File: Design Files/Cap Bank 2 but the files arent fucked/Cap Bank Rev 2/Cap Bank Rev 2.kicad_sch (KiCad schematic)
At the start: 20 parts, among them Q1 2N3904, Q2 2N3904, Q3 2N3904, Q4 2N3904

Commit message: New Cap Bank
wohooo
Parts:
- removed C2: C_Polarized, Library:bigcap, symbol Device:C_Polarized
- added C5: C_Polarized, Library:bigcap2pos, symbol Device:C_Polarized
- added J1: Conn_01x02, Library:xt30, symbol Connector_Generic:Conn_01x02
- C1: footprint Library:bigcap -> Library:bigcap2pos
- C3: footprint Library:bigcap -> Library:bigcap2neg
- C4: footprint Library:bigcap -> Library:smallcap
- C7: footprint Library:smallcap -> Library:bigcap2neg
- Q1, Q2, Q3, Q4: footprint Package_TO_SOT_THT:TO-92_Inline -> Library:2n3904
- renumbered C5 to C2
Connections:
- net V_IN: now also Q1.3 (C), R1.2, J1.1 (Pin_1); no longer C1.2, C2.2, C3.1, C3.2, C4.1, C4.2, C6.1, C6.2, C7.1, C7.2, C8.1, C8.2, Q1.2 (B), Q2.2 (B), Q3.2 (B), Q4.2 (B), R1.1, R2.1, R3.1, R4.1, R5.1, R6.1, R7.1, R8.1
- net at Q2.1 (E), R4.2: now also C3.2, C4.2, C6.1, Q3.3 (C), R5.2, C5.1
- net at Q4.3 (C), R7.2: now also C6.2, C7.1, C8.1, Q3.1 (E), R6.2, C5.2
- net at Q2.3 (C), R3.2: now also C1.2, C2.2, C3.1, C4.1, Q1.1 (E), R2.2
- net GND: now reaches Q4.1 (E), R8.2
- net GND: now also C7.2, C8.2, J1.2 (Pin_2)
- new net: Q3.2 (B), R5.1, R6.1
- new net: Q2.2 (B), R3.1, R4.1
- new net: Q1.2 (B), R1.1, R2.1
- new net: Q4.2 (B), R7.1, R8.1
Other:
- moved on the sheet: C1, Q1, R1, R2

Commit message: updated again!!!
ship it!
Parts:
- removed C2, C4, C6, C8: C_Polarized, Library:smallcap, symbol Device:C_Polarized
- added J2: Conn_01x02, Connector_AMASS:AMASS_XT30U-F_1x02_P5.0mm_Vertical, symbol Connector_Generic:Conn_01x02
- C1, C5: footprint Library:bigcap2pos -> Library:bigcap
- C3, C7: footprint Library:bigcap2neg -> Library:bigcap
- J1: footprint Library:xt30 -> Connector_AMASS:AMASS_XT30U-M_1x02_P5.0mm_Vertical
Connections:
- net GND: now also J1.1 (Pin_1), J2.1 (Pin_1); no longer J1.2 (Pin_2)
- net V_IN: now also J1.2 (Pin_2), J2.2 (Pin_2); no longer J1.1 (Pin_1)
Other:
- moved on the sheet: J1

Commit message: new bjt
who dis
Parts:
- removed Q1, Q2, Q3, Q4: 2N3904, Library:2n3904, symbol Transistor_BJT:2N3904
- added D1: LED, LED_THT:LED_D3.0mm_Clear, symbol Device:LED
- added Q1, Q2, Q3, Q4: TIP31, Library:tip31, symbol Transistor_BJT:TIP41
- added R9: 1000, Resistor_THT:R_Axial_DIN0207_L6.3mm_D2.5mm_P7.62mm_Horizontal, symbol Device:R
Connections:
- net GND: now also D1.1 (K), Q4.3 (E)
- net V_IN: now also Q1.2 (C), R9.1
- net at C7.1, R7.2: now also Q4.2 (C); no longer C5.2, R6.2
- net at R5.1, R6.1: now also Q3.1 (B)
- net at C5.1, R5.2: now also Q3.2 (C); no longer C3.2, R4.2
- net at R3.1, R4.1: now also Q2.1 (B)
- net at C3.1, R3.2: now also Q2.2 (C); no longer C1.2, R2.2
- net at R1.1, R2.1: now also Q1.1 (B)
- net at R7.1, R8.1: now also Q4.1 (B)
- new net: C5.2, Q3.3 (E), R6.2
- new net: C3.2, Q2.3 (E), R4.2
- new net: D1.2 (A), R9.2
- new net: C1.2, Q1.3 (E), R2.2

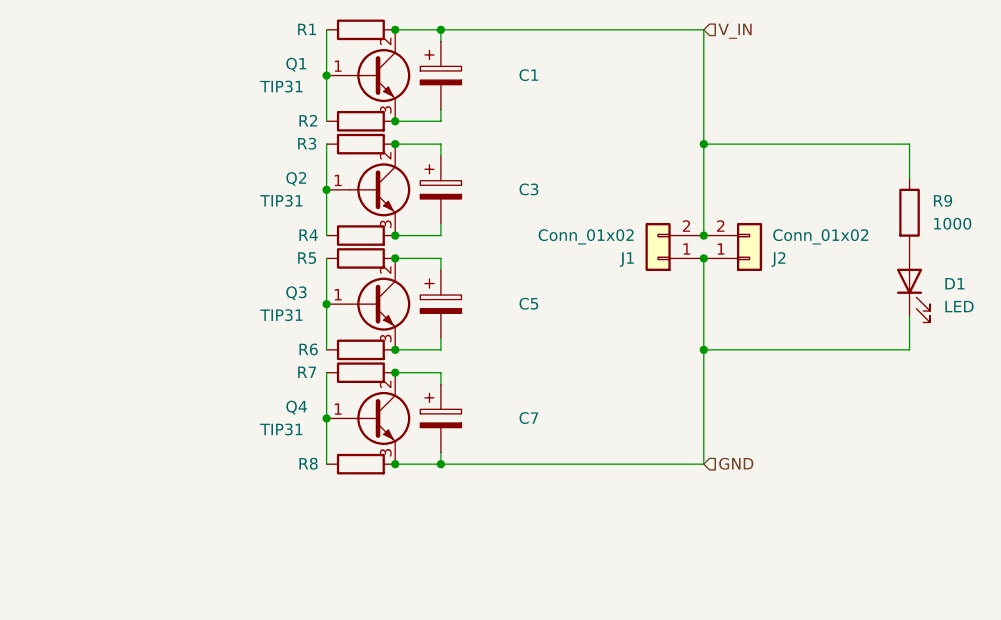
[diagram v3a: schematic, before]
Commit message: NO HEATSINKS
they were too large...
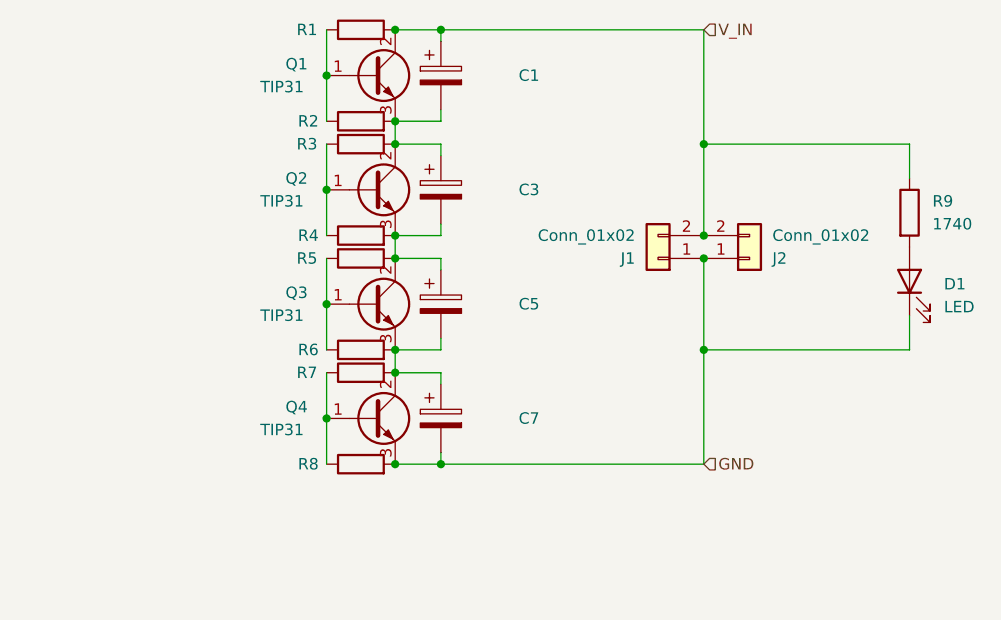
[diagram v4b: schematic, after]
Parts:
- Q1, Q2, Q3, Q4: footprint Library:tip31 -> Library:tip31sideways
- R9: value 1000 -> 1740
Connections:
- net at C7.1, Q4.2 (C), R7.2: now also C5.2, Q3.3 (E), R6.2
- net at C5.1, Q3.2 (C), R5.2: now also C3.2, Q2.3 (E), R4.2
- net at C3.1, Q2.2 (C), R3.2: now also C1.2, Q1.3 (E), R2.2
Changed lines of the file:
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@@
+	(wire
+		(pts
+			(xy 137.16 95.25) (xy 137.16 97.79)
+		)
+		(stroke
+			(width 0)
+			(type default)
+		)
+	)
 	(wire
 		(pts
@@
 	(wire
 		(pts
+			(xy 137.16 82.55) (xy 137.16 85.09)
+		)
+		(stroke
+			(width 0)
+			(type default)
+		)
+	)
+	(wire
+		(pts
 			(xy 137.16 82.55) (xy 142.24 82.55)
 		)
@@
 		(pts
 			(xy 137.16 85.09) (xy 142.24 85.09)
+		)
+		(stroke
+			(width 0)
+			(type default)
+		)
+	)
+	(wire
+		(pts
+			(xy 137.16 107.95) (xy 137.16 110.49)
 		)
 		(stroke
@@
 			)
 		)
-		(property "Footprint" "Library:tip31"
+		(property "Footprint" "Library:tip31sideways"
 			(at 140.97 117.475 0)
 			(effects
@@
 			)
 		)
-		(property "Footprint" "Library:tip31"
+		(property "Footprint" "Library:tip31sideways"
 			(at 140.97 104.775 0)
 			(effects
@@
 			)
 		)
-		(property "Value" "1000"
+		(property "Value" "1740"
 			(at 196.85 93.9799 0)
 			(effects
@@
 			)
 		)
-		(property "Footprint" "Library:tip31"
+		(property "Footprint" "Library:tip31sideways"
 			(at 140.97 92.075 0)
 			(effects
@@
 			)
 		)
-		(property "Footprint" "Library:tip31"
+		(property "Footprint" "Library:tip31sideways"
 			(at 140.97 79.375 0)
 			(effects
